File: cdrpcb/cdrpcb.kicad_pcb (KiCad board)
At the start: 2 copper layers, 40 parts, among them J1 Conn_02x04_Odd_Even, J2 Conn_01x03, J3 Conn_01x03, J4 Conn_01x03, J5 Conn_01x03, J6 Conn_01x03, J7 Conn_01x06, J8 Conn_01x05, J9 Conn_01x03, SW1 SW_Push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

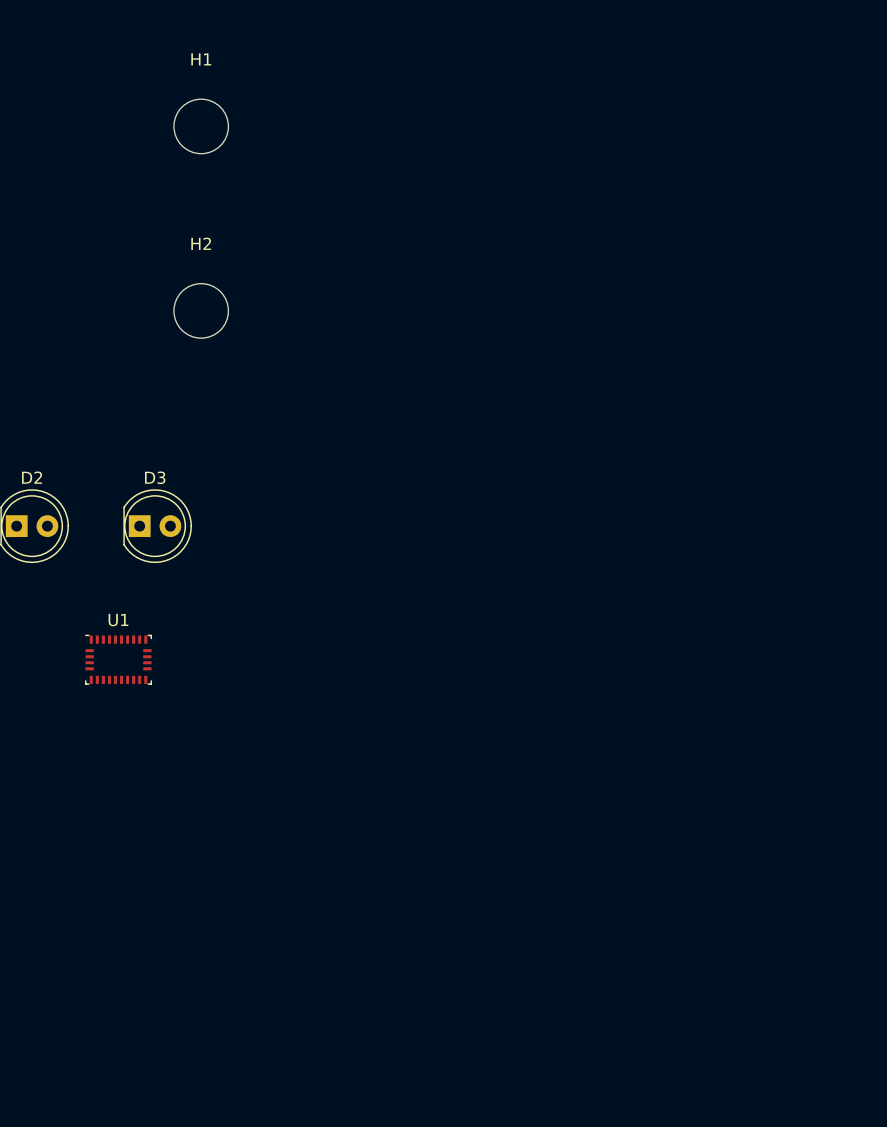
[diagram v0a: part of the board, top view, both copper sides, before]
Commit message: update cdrpcb
bno055 footprints
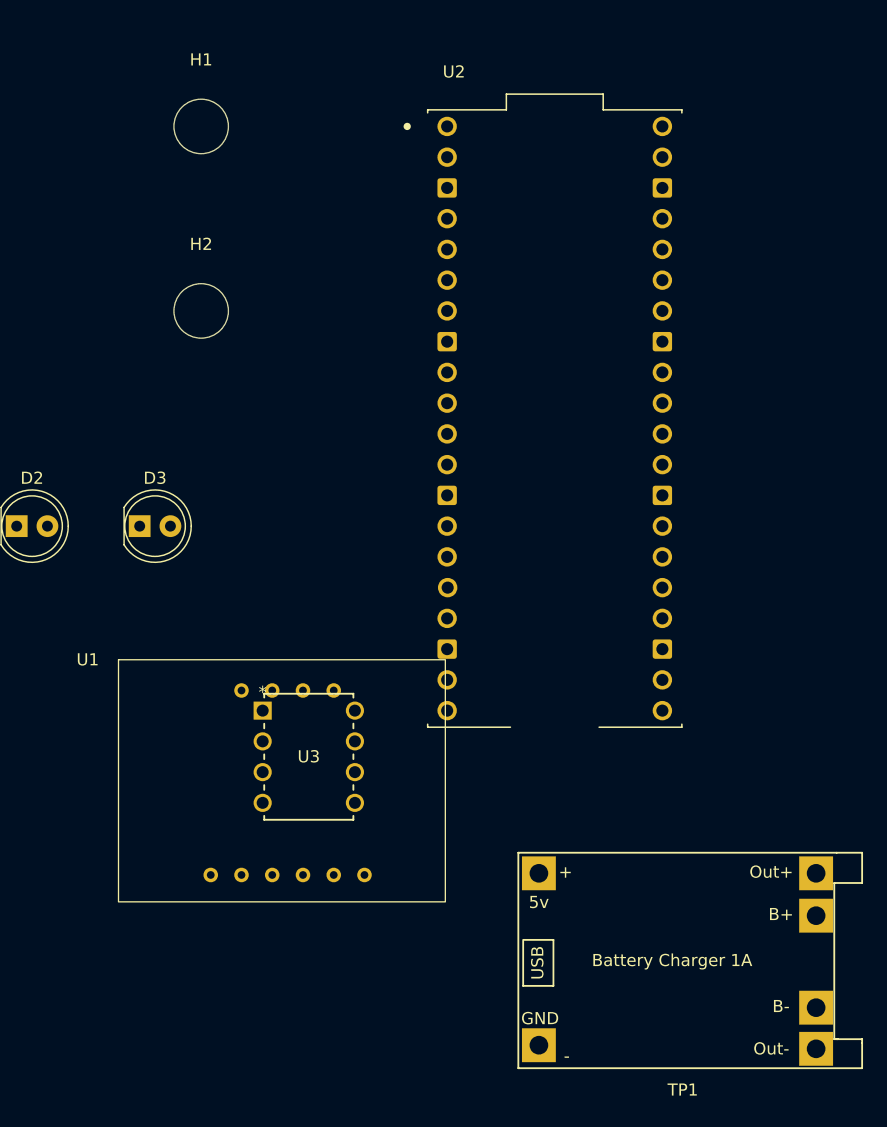
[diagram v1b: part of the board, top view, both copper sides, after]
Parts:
- added TP1: ~, TP4056:TP4056-18650, F.Cu at (186.2, 110.8)
- added U2: SC0918, RP2040_SC0918:MODULE_SC0918, F.Cu at (189.2, 74.9)
- added U3: 25LC1024-I/P, 25LC1024:PDIP8_300MC_MCH, F.Cu at (165.1, 99.1)
- U1: footprint Package_LGA:LGA-28_5.2x3.8mm_P0.5mm -> Library:BNO055_Breakout
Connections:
- R10 pad 1: Net-(R10-Pad1) -> unconnected-(R10-Pad1)
- R13 pad 1: Net-(R13-Pad1) -> unconnected-(R13-Pad1)
- R4 pad 1: Net-(R4-Pad1) -> unconnected-(R4-Pad1)
- R6 pad 1: Net-(R6-Pad1) -> unconnected-(R6-Pad1)
- R8 pad 1: Net-(R8-Pad1) -> unconnected-(R8-Pad1)

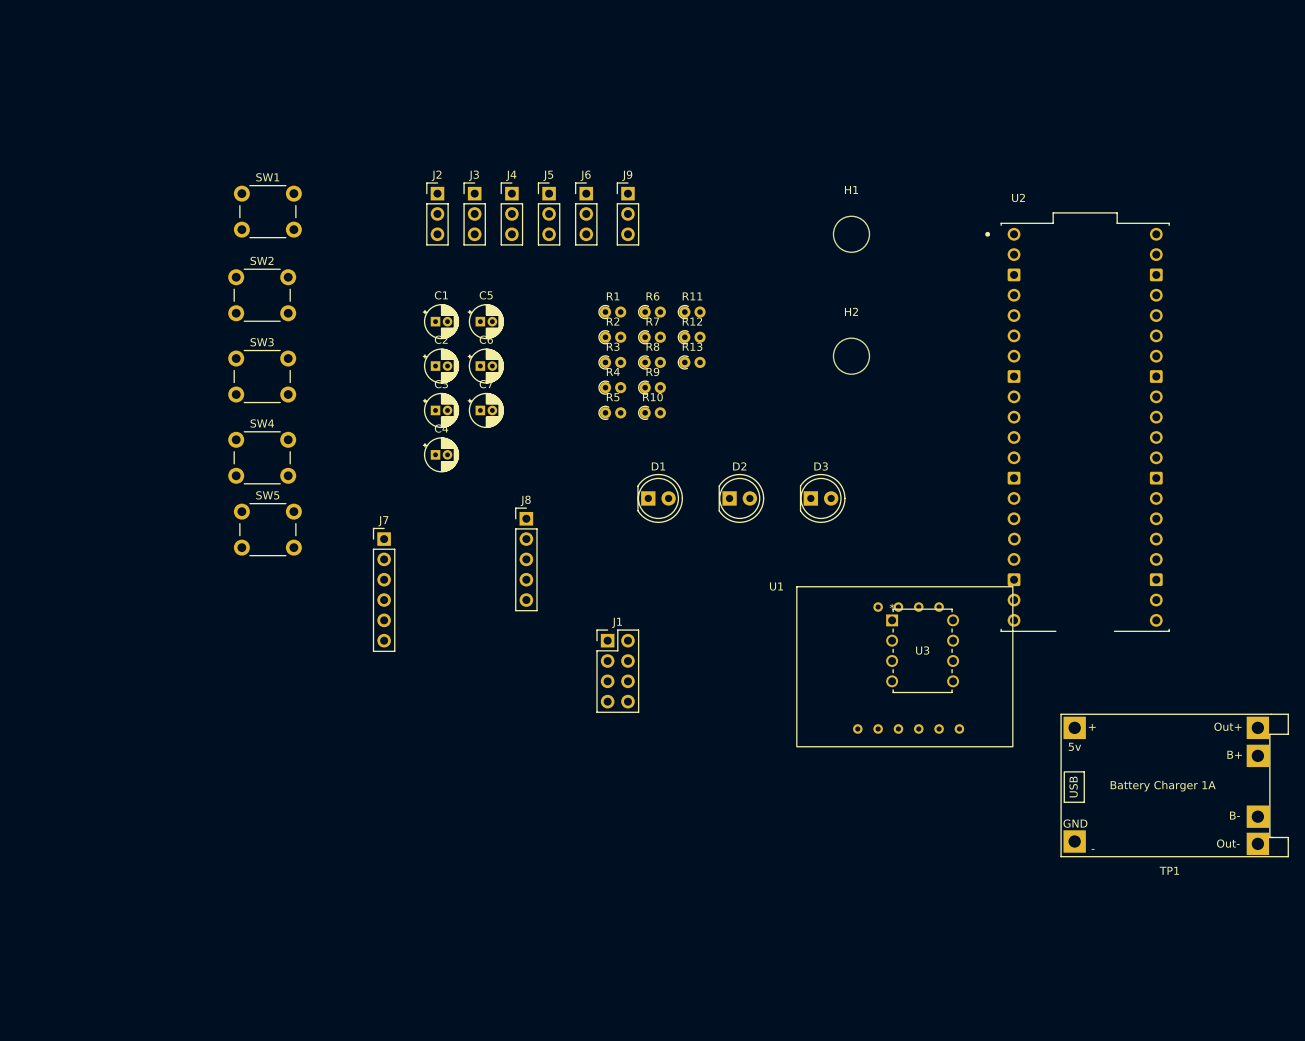
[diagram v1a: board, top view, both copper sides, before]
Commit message: cdrpcb3
Started routing
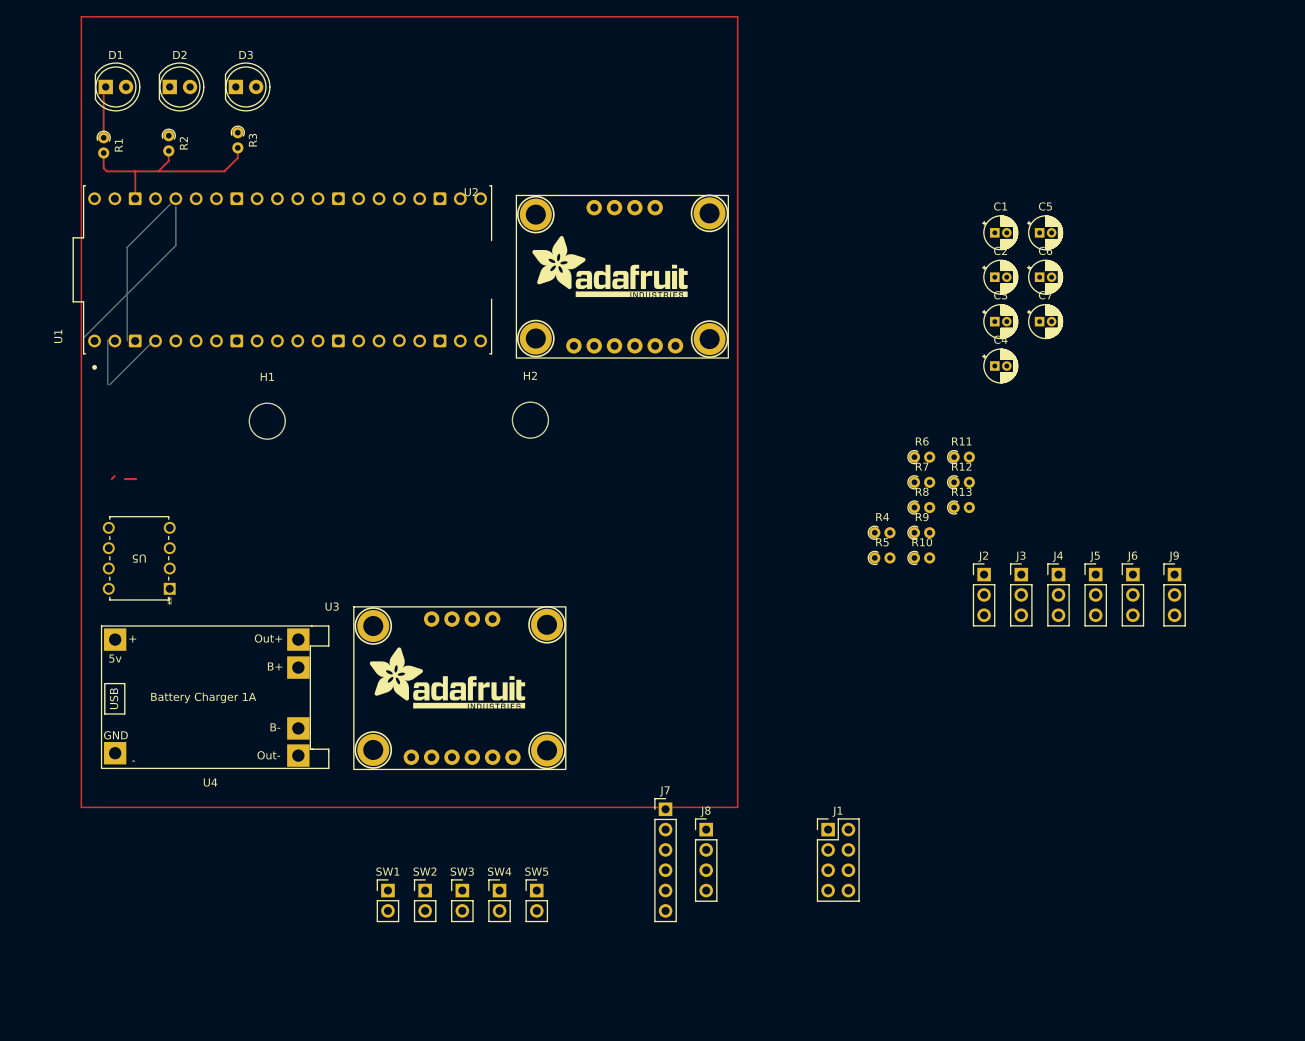
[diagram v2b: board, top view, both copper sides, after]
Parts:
- removed TP1: ~, TP4056:TP4056-18650
- removed the U1 at (153.2, 94.9)
- added U2: ~, Library:BNO055_Breakout, F.Cu at (118.0, 45.9)
- added U3: ~, Library:BNO055_Breakout, F.Cu at (97.6, 97.4)
- added U4: ~, TP4056:TP4056-18650, F.Cu at (66.3, 99.8)
- J8: value Conn_01x05 -> Conn_01x04; footprint Connector_PinHeader_2.54mm:PinHeader_1x05_P2.54mm_Vertical -> Connector_PinHeader_2.54mm:PinHeader_1x04_P2.54mm_Vertical
- SW1, SW2, SW3, SW4, SW5: value SW_Push -> Conn_01x02_Pin; footprint Button_Switch_THT:SW_PUSH_6mm -> Connector_PinHeader_2.54mm:PinHeader_1x02_P2.54mm_Vertical
- moved U1 101.6 mm to (89.5, 55.2), turned to 90 degrees
- moved U5 90.4 mm to (74.8, 95.1), turned to 180 degrees
- moved SW1 89.0 mm to (102.1, 132.8)
- moved D3 88.4 mm to (83.1, 32.4)
- moved D2 86.8 mm to (74.8, 32.4)
- moved D1 85.1 mm to (66.8, 32.4)
- moved J2 83.3 mm to (176.6, 93.3)
- moved J3 83.3 mm to (181.2, 93.3)
- moved J4 83.3 mm to (185.9, 93.3)
- moved J5 83.3 mm to (190.5, 93.3)
- moved J6 83.3 mm to (195.2, 93.3)
- moved J9 83.3 mm to (200.4, 93.3)
- moved SW2 80.2 mm to (106.7, 132.8)
- moved H1 76.7 mm to (87.0, 74.2)
- moved SW3 72.3 mm to (111.4, 132.8)
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- renumbered U2 to U1, U3 to U5
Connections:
- J8 pad 2: /I2C1_SDA -> /GP6_INT
- J8 pad 3: /I2C1_SCL -> GND
- J8 pad 4: GND -> +3.3V
- R10 pad 1: unconnected-(R10-Pad1) -> Net-(SW4-Pin_2)
- R13 pad 1: unconnected-(R13-Pad1) -> Net-(SW5-Pin_2)
- R4 pad 1: unconnected-(R4-Pad1) -> Net-(SW1-Pin_2)
- R6 pad 1: unconnected-(R6-Pad1) -> Net-(SW2-Pin_2)
- R8 pad 1: unconnected-(R8-Pad1) -> Net-(SW3-Pin_2)
- SW1 pad 1: Net-(R4-Pad1) -> /RST
- SW1 pad 2: /RST -> Net-(SW1-Pin_2)
- SW2 pad 1: Net-(R6-Pad1) -> /SW0
- SW2 pad 2: /SW0 -> Net-(SW2-Pin_2)
- SW3 pad 1: Net-(R8-Pad1) -> /SW1
- SW3 pad 2: /SW1 -> Net-(SW3-Pin_2)
- SW4 pad 1: Net-(R10-Pad1) -> /SW2
- SW4 pad 2: /SW2 -> Net-(SW4-Pin_2)
- SW5 pad 1: Net-(R13-Pad1) -> /SW2
- SW5 pad 2: /SW2 -> Net-(SW5-Pin_2)
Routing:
- net (no net): track 0.00 -> 40.3 mm
- net GND: track 0.00 -> 28.7 mm
- net /SPI0_SCK: track 0.00 -> 7.21 mm
- net Net-(D1-K): track 0.00 -> 6.98 mm
- net /GP0_UART0_TX: track 0.00 -> 5.59 mm

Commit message: cdrpcb4
Routed the PCB
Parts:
- removed C6, C7: 100nF, Capacitor_THT:CP_Radial_D4.0mm_P1.50mm
- moved C1 97.3 mm to (96.1, 103.2)
- moved J1 94.3 mm to (63.3, 135.2)
- moved SW2 74.7 mm to (139.1, 65.6)
- moved R4 72.9 mm to (90.7, 97.7)
- moved SW4 72.6 mm to (158.6, 74.0)
- moved U3 70.2 mm to (148.7, 145.5), turned to 90 degrees
- moved R5 67.7 mm to (95.5, 97.7)
- moved D1 64.4 mm to (62.5, 96.7)
- moved D3 64.4 mm to (78.8, 96.7)
- moved R1 64.4 mm to (62.3, 103.0)
- moved D2 64.4 mm to (70.5, 96.7)
- moved R2 64.4 mm to (70.4, 102.8)
- moved R3 64.4 mm to (79.0, 102.4)
- moved U1 64.4 mm to (85.3, 119.5)
- moved U2 60.8 mm to (135.4, 104.1), turned to -90 degrees
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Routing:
- net GND: track 28.7 -> 422.8 mm
- net +3.3V: track 0.46 -> 218.4 mm
- net /GP28_ADC2: track 0.00 -> 135.1 mm
- net GNDA: track 0.00 -> 131.7 mm, vias 0 -> 1
- net /RST: track 0.00 -> 111.7 mm
- net VDDA: track 0.00 -> 110.7 mm, vias 0 -> 1
- net +5V: track 0.00 -> 109.0 mm
- net +3V3: track 0.00 -> 108.3 mm, vias 0 -> 1
- net /SW2: track 0.00 -> 105.8 mm, vias 0 -> 1
- net /GP27_ADC1: track 0.00 -> 100.6 mm, vias 0 -> 1
- net /SW0: track 0.00 -> 97.1 mm
- net /GP8_UART1_TX: track 0.00 -> 81.9 mm, vias 0 -> 2
- net /I2C1_SDA: track 0.00 -> 74.9 mm, vias 0 -> 1
- net /SPI0_SCK: track 7.21 -> 81.1 mm
- net /GP1_UART0_RX: track 0.00 -> 72.5 mm, vias 0 -> 1
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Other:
- board outline added: 119.8 x 90.3 mm

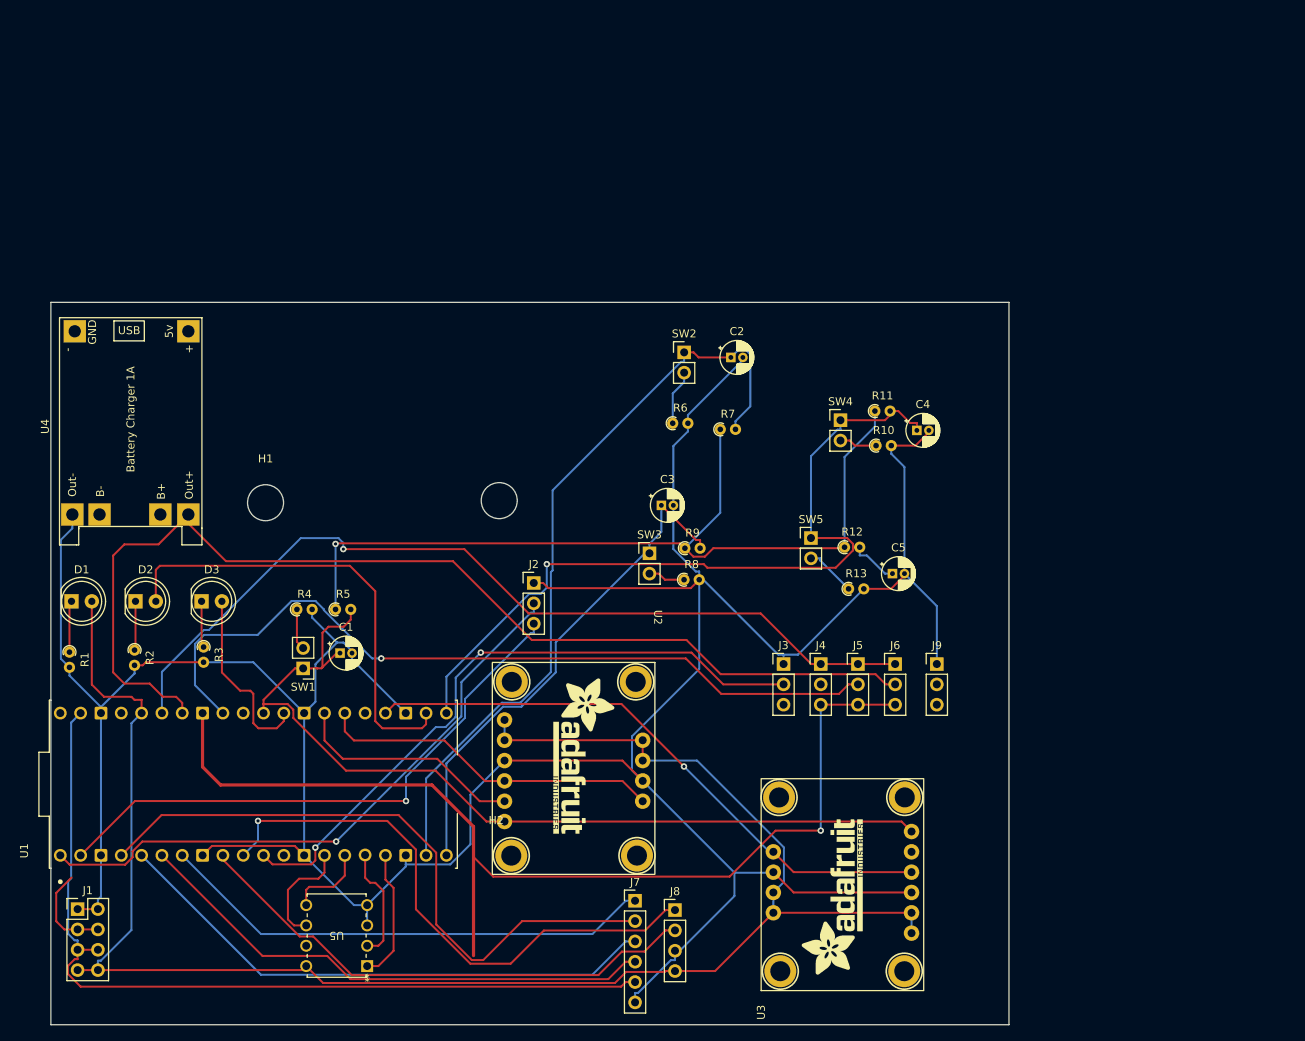
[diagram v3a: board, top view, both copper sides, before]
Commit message: cdrpcb5
centered the mounting holes
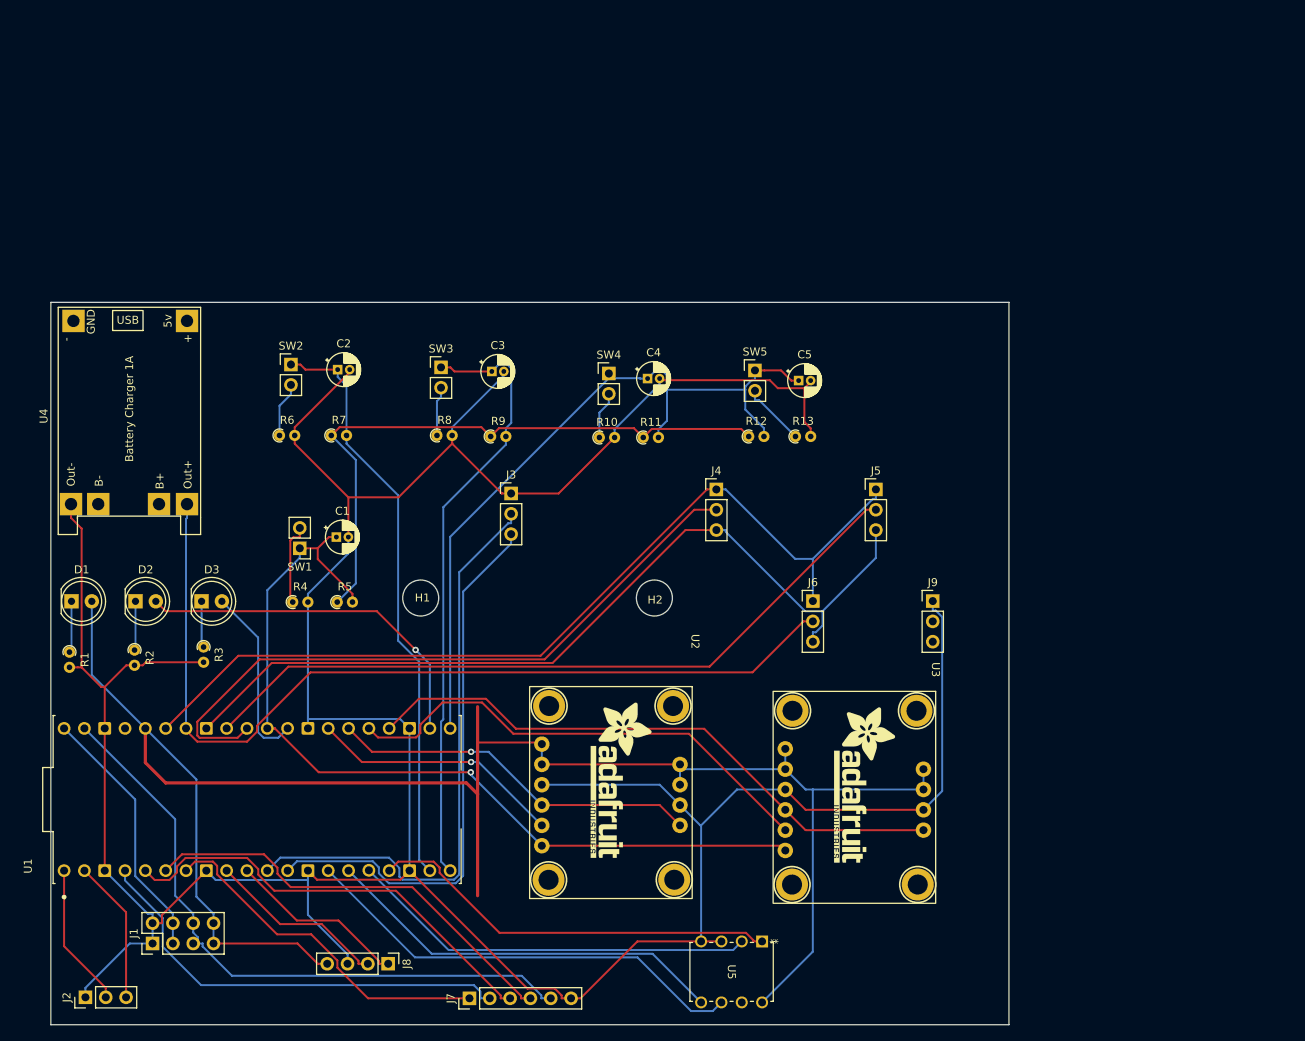
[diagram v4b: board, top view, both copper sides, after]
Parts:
- moved J2 76.3 mm to (64.3, 146.2), turned to 90 degrees
- moved U5 49.5 mm to (148.8, 139.2), turned to -90 degrees
- moved R6 49.2 mm to (88.5, 75.9)
- moved SW2 49.2 mm to (90.0, 67.1)
- moved C2 49.2 mm to (95.8, 67.7)
- moved R7 48.6 mm to (95.0, 75.9)
- moved U3 43.6 mm to (170.5, 107.8), turned to -90 degrees
- moved J3 40.2 mm to (117.5, 83.2)
- moved J8 36.5 mm to (102.1, 142.0), turned to -90 degrees
- moved R8 35.8 mm to (108.2, 75.9)
- moved SW3 34.9 mm to (108.7, 67.4)
- moved R10 34.6 mm to (128.5, 76.2)
- moved C4 34.3 mm to (134.5, 68.8)
- moved SW4 29.5 mm to (129.7, 68.2)
- moved R11 29.1 mm to (134.0, 76.2)
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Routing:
- net /GP26_ADC0: track 0.00 -> 84.4 mm
- net /GP9_UART1_RX: track 0.00 -> 69.6 mm
- net /I2C1_SCL: track 0.00 -> 61.6 mm
- net /GP0_UART0_TX: track 76.8 -> 18.0 mm, vias 1 -> 0
- net /GP1_UART0_RX: track 72.5 -> 18.0 mm, vias 1 -> 0
- net /GP7_AD0: track 71.7 -> 22.7 mm, vias 1 -> 0
- net /SPI1_SCK: track 13.9 -> 56.9 mm
- net /GP6_INT: track 65.3 -> 22.7 mm
- net /SPI1_MOSI: track 10.0 -> 50.9 mm
- net /SPI1_MISO: track 14.3 -> 51.2 mm
- net /SPI1_CS: track 16.5 -> 51.7 mm
- net GND: track 422.8 -> 453.8 mm
- net +3V3: track 108.3 -> 77.9 mm, vias 1 -> 0
- net +5V: track 109.0 -> 80.7 mm
- net /SPI0_SCK: track 81.1 -> 55.5 mm
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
